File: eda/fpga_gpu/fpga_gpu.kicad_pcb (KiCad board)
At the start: 2 copper layers, 94.5 x 68.3 mm, 57 parts, among them J1 VGA, J2 Bus expansion, U1 ICE40HX4K-TQ144, U2 SST25VF080B-50-4x-S2Ax, U3 74HCT541, U4 74HCT541, U5 74HCT541, U6 TXS0108EPW, U7 TXS0108EPW, U8 AMS1117-3.3, U9 AP2112K-1.2, X1 TXC-7C

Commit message: GPU routing
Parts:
- added U10: IS61C5128AL-10KLI, Package_SO:SOJ-36_10.16x23.49mm_P1.27mm, F.Cu at (43.2, 106.4)
- moved D1 21.8 mm to (60.7, 68.6), turned to 0 degrees
- moved C12 20.8 mm to (43.7, 80.6), turned to 0 degrees
- moved C1 13.5 mm to (56.2, 91.3)
- moved C10 13.5 mm to (65.8, 110.5)
- moved C4 13.5 mm to (63.2, 107.5)
- moved C5 13.5 mm to (74.1, 107.6)
- moved C6 13.5 mm to (83.6, 93.8)
- moved C7 13.5 mm to (56.2, 93.3)
- moved C9 13.5 mm to (83.6, 85.2)
- moved R12 13.5 mm to (90.6, 111.8)
- moved R13 13.5 mm to (90.4, 109.7)
- moved R14 13.5 mm to (90.4, 107.7)
- moved R2 13.5 mm to (92.5, 81.8)
- moved R3 13.5 mm to (94.5, 81.8)
- moved R4 13.5 mm to (90.4, 81.8)
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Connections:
- U1 pad 110: /Interfacing/ADev0 -> /Interfacing/ADev3
- U1 pad 112: /Interfacing/ADev1 -> /Interfacing/ADev2
- U1 pad 113: /Interfacing/ADev2 -> /Interfacing/ADev1
- U1 pad 114: /Interfacing/ADev3 -> /Interfacing/ADev0
- U3 pad 2: /Interfacing/Expansion/A0 -> /Interfacing/Expansion/A3
- U3 pad 3: /Interfacing/Expansion/A1 -> /Interfacing/Expansion/A2
- U3 pad 4: /Interfacing/Expansion/A2 -> /Interfacing/Expansion/A1
- U3 pad 5: /Interfacing/Expansion/A3 -> /Interfacing/Expansion/A0
- U5 pad 11: /Interfacing/Expansion/D7 -> /Interfacing/Expansion/D0
- U5 pad 12: /Interfacing/Expansion/D6 -> /Interfacing/Expansion/D1
- U5 pad 13: /Interfacing/Expansion/D5 -> /Interfacing/Expansion/D2
- U5 pad 14: /Interfacing/Expansion/D4 -> /Interfacing/Expansion/D3
- U5 pad 15: /Interfacing/Expansion/D3 -> /Interfacing/Expansion/D4
- U5 pad 16: /Interfacing/Expansion/D2 -> /Interfacing/Expansion/D5
- U5 pad 17: /Interfacing/Expansion/D1 -> /Interfacing/Expansion/D6
- U5 pad 18: /Interfacing/Expansion/D0 -> /Interfacing/Expansion/D7
- U5 pad 2: /DOut0 -> /DOut7
- U5 pad 3: /DOut1 -> /DOut6
- U5 pad 4: /DOut2 -> /DOut5
- U5 pad 5: /DOut3 -> /DOut4
- U5 pad 6: /DOut4 -> /DOut3
- U5 pad 7: /DOut5 -> /DOut2
- U5 pad 8: /DOut6 -> /DOut1
- U5 pad 9: /DOut7 -> /DOut0
- U7 pad 16: /Interfacing/ADev3 -> /Interfacing/ADev0
- U7 pad 17: /Interfacing/ADev2 -> /Interfacing/ADev1
- U7 pad 18: /Interfacing/ADev1 -> /Interfacing/ADev2
- U7 pad 20: /Interfacing/ADev0 -> /Interfacing/ADev3
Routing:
- net GND: track 5.31 -> 73.2 mm, vias 0 -> 7
- net /DIn0: track 0.00 -> 47.3 mm
- net /DIn1: track 0.00 -> 46.2 mm
- net /DIn2: track 0.00 -> 45.2 mm
- net VCC: track 8.34 -> 52.7 mm
- net /DIn3: track 0.00 -> 44.3 mm
- net +3.3V: track 0.00 -> 43.4 mm
- net /DIn4: track 0.00 -> 43.1 mm
- net /DIn7: track 0.00 -> 42.3 mm
- net /DIn5: track 0.00 -> 41.9 mm
- net /DIn6: track 0.00 -> 40.9 mm
- net /Interfacing/Expansion/A0: track 0.00 -> 40.6 mm
- net /Interfacing/Expansion/A1: track 0.00 -> 33.3 mm
- net /DOut0: track 0.00 -> 33.3 mm
- net /DOut1: track 0.00 -> 32.4 mm
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- added copper zone on B.Cu, net GND

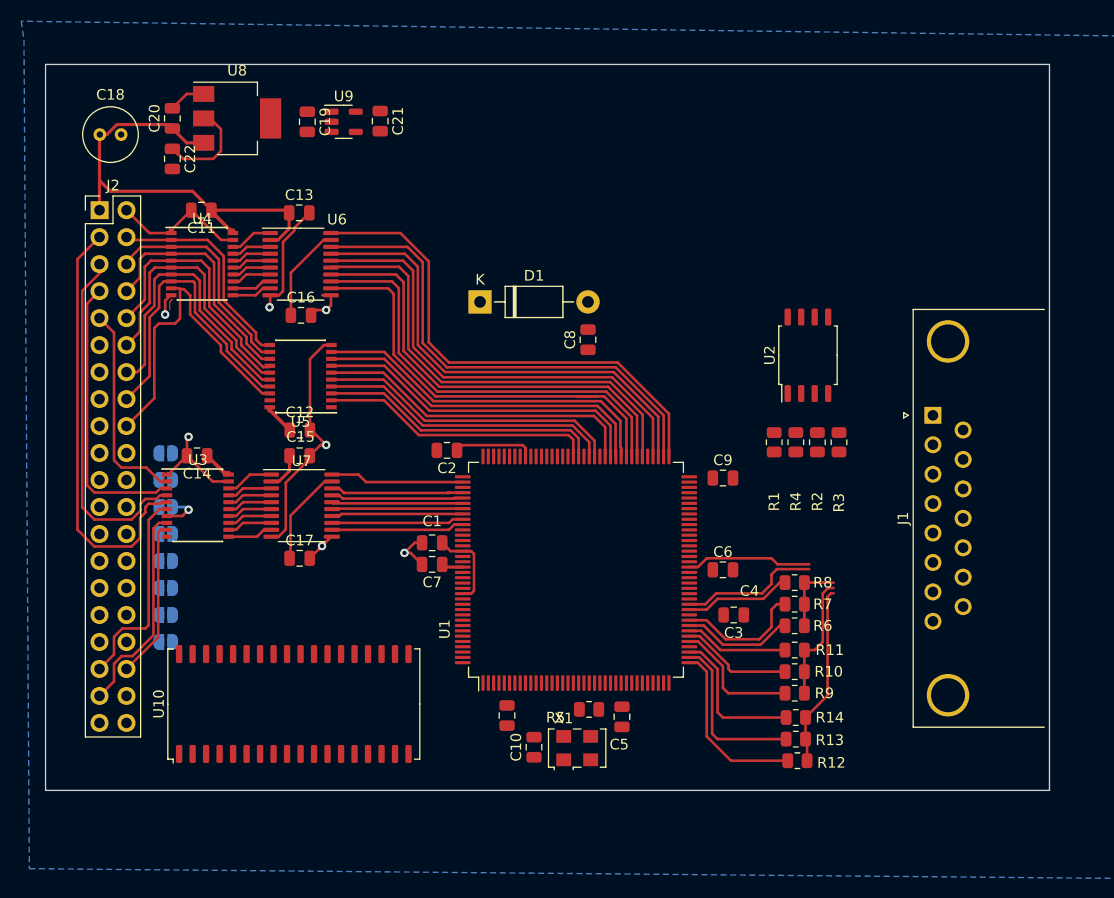
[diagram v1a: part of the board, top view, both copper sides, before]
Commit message: More routing on the GPU board
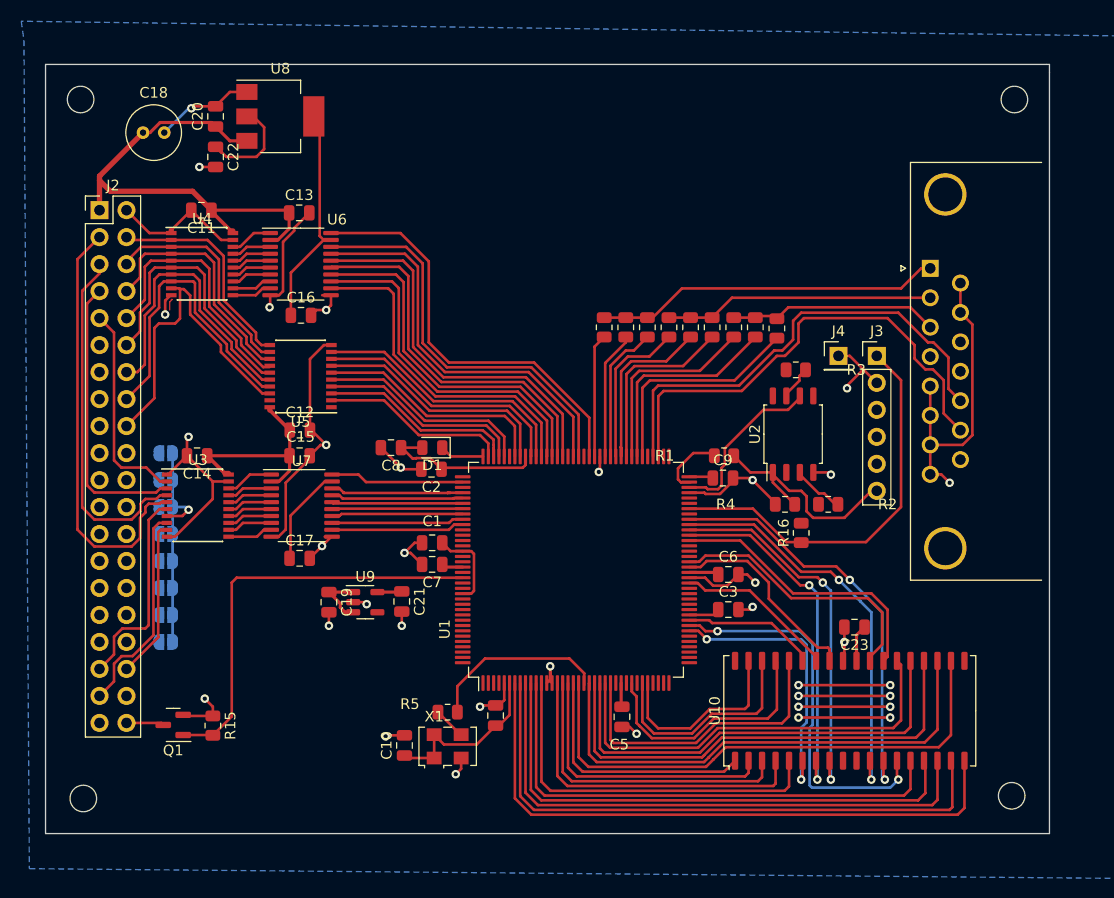
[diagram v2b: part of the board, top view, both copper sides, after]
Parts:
- added C23: 100n, Capacitor_SMD:C_0805_2012Metric, F.Cu at (95.9, 99.2)
- added H1: MountingHole, MountingHole:MountingHole_2.5mm, F.Cu at (111.0, 49.5)
- added H2: MountingHole, MountingHole:MountingHole_2.5mm, F.Cu at (23.1, 49.5)
- added H3: MountingHole, MountingHole:MountingHole_2.5mm, F.Cu at (110.7, 115.1)
- added H4: MountingHole, MountingHole:MountingHole_2.5mm, F.Cu at (23.4, 115.3)
- added J3: programming, Connector_PinHeader_2.54mm:PinHeader_1x06_P2.54mm_Vertical, F.Cu at (98.0, 73.7)
- added J4: reset ground, Connector_PinHeader_2.54mm:PinHeader_1x01_P2.54mm_Vertical, F.Cu at (94.4, 73.7)
- added Q1: 2N7002, Package_TO_SOT_SMD:SOT-23, F.Cu at (31.8, 108.4)
- added R15: 10k, Resistor_SMD:R_0805_2012Metric, F.Cu at (35.6, 108.5)
- added R16: 10k, Resistor_SMD:R_0805_2012Metric, F.Cu at (90.9, 90.3)
- D1: footprint Diode_THT:D_DO-41_SOD81_P10.16mm_Horizontal -> Diode_SMD:D_0805_2012Metric
- moved U10 52.3 mm to (95.5, 107.1)
- moved C19 45.3 mm to (46.5, 96.8)
- moved C21 45.3 mm to (53.3, 96.8)
- moved U9 45.3 mm to (49.9, 96.8)
- moved R12 40.7 mm to (88.6, 71.1), turned to -90 degrees
- moved R13 38.9 mm to (86.6, 71.0), turned to -90 degrees
- moved R14 37.2 mm to (84.6, 71.0), turned to -90 degrees
- moved R9 35.3 mm to (82.5, 71.0), turned to -90 degrees
- moved R10 33.9 mm to (80.5, 71.0), turned to -90 degrees
- moved R11 32.6 mm to (78.5, 71.0), turned to -90 degrees
- moved R6 31.3 mm to (76.5, 71.0), turned to -90 degrees
- moved R7 30.5 mm to (74.4, 71.0), turned to -90 degrees
- moved R8 30.0 mm to (72.4, 71.0), turned to -90 degrees
- moved C8 21.1 mm to (52.3, 82.3), turned to 180 degrees
- moved D1 14.4 mm to (56.2, 82.3), turned to 180 degrees
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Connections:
- J1 pad 13: /HSYNC -> /VSYNC
- J1 pad 14: /VSYNC -> /HSYNC
- J2 pad 40: /Interfacing/Expansion/~{IRQ} -> /Interfacing/~{IRQ}
- U1 pad 10: unconnected-(U1D-IOL_5B-Pad10) -> /RamA6
- U1 pad 101: unconnected-(U1B-IOR_160-Pad101) -> /DOut2
- U1 pad 102: unconnected-(U1B-IOR_161-Pad102) -> /DOut3
- U1 pad 104: unconnected-(U1B-IOR_164-Pad104) -> /DOut4
- U1 pad 105: unconnected-(U1B-IOR_165-Pad105) -> /DOut5
- U1 pad 106: unconnected-(U1B-IOR_166-Pad106) -> /DOut6
- U1 pad 107: unconnected-(U1B-IOR_167-Pad107) -> /DOut7
- U1 pad 11: unconnected-(U1D-IOL_8A-Pad11) -> /RamA5
- U1 pad 12: unconnected-(U1D-IOL_8B-Pad12) -> /RamA4
- U1 pad 128: unconnected-(U1A-IOT_197_GBIN1-Pad128) -> /FpgaIRQ
- U1 pad 15: unconnected-(U1D-IOL_10A-Pad15) -> /RamA3
- U1 pad 16: unconnected-(U1D-IOL_10B-Pad16) -> /RamA2
- U1 pad 17: unconnected-(U1D-IOL_12A-Pad17) -> /RamA1
- U1 pad 18: unconnected-(U1D-IOL_12B-Pad18) -> /RamA0
- U1 pad 19: unconnected-(U1D-IOL_13A-Pad19) -> /RamA10
- U1 pad 21: unconnected-(U1D-IOL_14A_GBIN6-Pad21) -> /RamA11
- U1 pad 22: unconnected-(U1D-IOL_14B-Pad22) -> /RamA12
- U1 pad 23: unconnected-(U1D-IOL_17A-Pad23) -> /RamA13
- U1 pad 24: unconnected-(U1D-IOL_17B-Pad24) -> /RamA14
- U1 pad 25: unconnected-(U1D-IOL_18A-Pad25) -> /RamA15
- U1 pad 29: unconnected-(U1D-IOL_23B-Pad29) -> /RamA16
- U1 pad 31: unconnected-(U1D-IOL_24A-Pad31) -> /RamA17
- U1 pad 32: unconnected-(U1D-IOL_24B-Pad32) -> /RamA18
- U1 pad 37: /VGA Connector/Blue0 -> unconnected-(U1C-IOB_56-Pad37)
- U1 pad 38: /VGA Connector/Blue1 -> unconnected-(U1C-IOB_57-Pad38)
- U1 pad 39: /VGA Connector/Blue2 -> unconnected-(U1C-IOB_61-Pad39)
- U1 pad 41: /VGA Connector/Green0 -> unconnected-(U1C-IOB_63-Pad41)
- U1 pad 42: /VGA Connector/Green1 -> unconnected-(U1C-IOB_64-Pad42)
- U1 pad 43: /VGA Connector/Green2 -> /~{RamCE}
- U1 pad 44: /VGA Connector/Red0 -> /~{RamWE}
- U1 pad 45: /VGA Connector/Red1 -> /~{RamOE}
- U1 pad 47: /VGA Connector/Red2 -> unconnected-(U1C-IOB_79-Pad47)
- U1 pad 48: /VSYNC -> unconnected-(U1C-IOB_80-Pad48)
- U1 pad 52: unconnected-(U1C-IOB_82_GBIN4-Pad52) -> /RamIo7
- U1 pad 55: /HSYNC -> /RamIo6
- U1 pad 56: unconnected-(U1C-IOB_94-Pad56) -> /RamIo5
- U1 pad 60: unconnected-(U1C-IOB_95-Pad60) -> /RamIo4
- U1 pad 61: unconnected-(U1C-IOB_96-Pad61) -> /RamIo0
- U1 pad 62: unconnected-(U1C-IOB_102-Pad62) -> /RamIo1
- U1 pad 63: unconnected-(U1C-IOB_103_CBSEL0-Pad63) -> /RamIo2
- U1 pad 64: unconnected-(U1C-IOB_104_CBSEL1-Pad64) -> /RamIo3
- U1 pad 7: unconnected-(U1D-IOL_4A-Pad7) -> /RamA9
- U1 pad 73: /DIn0 -> unconnected-(U1B-IOR_109-Pad73)
- U1 pad 74: /DIn1 -> unconnected-(U1B-IOR_110-Pad74)
- U1 pad 75: /DIn2 -> /HSYNC
- U1 pad 76: /DIn3 -> /VSYNC
- U1 pad 78: /DIn4 -> /VGA Connector/Blue0
- U1 pad 79: /DIn5 -> /VGA Connector/Blue1
- U1 pad 8: unconnected-(U1D-IOL_4B-Pad8) -> /RamA8
- U1 pad 80: /DIn6 -> /VGA Connector/Blue2
- U1 pad 81: /DIn7 -> /VGA Connector/Green0
- U1 pad 82: /DOut0 -> /VGA Connector/Green1
- U1 pad 83: /DOut1 -> /VGA Connector/Green2
- U1 pad 84: /DOut2 -> /VGA Connector/Red0
- U1 pad 85: /DOut3 -> /VGA Connector/Red1
- U1 pad 87: /DOut4 -> /VGA Connector/Red2
- U1 pad 88: /DOut5 -> /DIn0
- U1 pad 9: unconnected-(U1D-IOL_5A-Pad9) -> /RamA7
- U1 pad 90: /DOut6 -> /DIn1
- U1 pad 91: /DOut7 -> /DIn2
- U1 pad 93: unconnected-(U1B-IOR_140_GBIN3-Pad93) -> /DIn3
- U1 pad 94: unconnected-(U1B-IOR_141_GBIN2-Pad94) -> /DIn4
- U1 pad 95: unconnected-(U1B-IOR_144-Pad95) -> /DIn5
- U1 pad 96: unconnected-(U1B-IOR_146-Pad96) -> /DIn6
- U1 pad 97: unconnected-(U1B-IOR_147-Pad97) -> /DIn7
- U1 pad 98: unconnected-(U1B-IOR_148-Pad98) -> /DOut0
- U1 pad 99: unconnected-(U1B-IOR_152-Pad99) -> /DOut1
- U10 pad 1: unconnected-(U10-A0-Pad1) -> /RamA0
- U10 pad 11: unconnected-(U10-I/O2-Pad11) -> /RamIo2
- U10 pad 12: unconnected-(U10-I/O3-Pad12) -> /RamIo3
- U10 pad 13: unconnected-(U10-~{WE}-Pad13) -> /~{RamWE}
- U10 pad 14: unconnected-(U10-A5-Pad14) -> /RamA5
- U10 pad 15: unconnected-(U10-A6-Pad15) -> /RamA6
- U10 pad 16: unconnected-(U10-A7-Pad16) -> /RamA7
- U10 pad 17: unconnected-(U10-A8-Pad17) -> /RamA8
- U10 pad 18: unconnected-(U10-A9-Pad18) -> /RamA9
- U10 pad 2: unconnected-(U10-A1-Pad2) -> /RamA1
- U10 pad 20: unconnected-(U10-A10-Pad20) -> /RamA10
- U10 pad 21: unconnected-(U10-A11-Pad21) -> /RamA11
- U10 pad 22: unconnected-(U10-A12-Pad22) -> /RamA12
- U10 pad 23: unconnected-(U10-A13-Pad23) -> /RamA13
- U10 pad 24: unconnected-(U10-A14-Pad24) -> /RamA14
- U10 pad 25: unconnected-(U10-I/O4-Pad25) -> /RamIo4
- U10 pad 26: unconnected-(U10-I/O5-Pad26) -> /RamIo5
- U10 pad 27: Net-(U10-VDD-Pad27) -> VCC
- U10 pad 29: unconnected-(U10-I/O6-Pad29) -> /RamIo6
- U10 pad 3: unconnected-(U10-A2-Pad3) -> /RamA2
- U10 pad 30: unconnected-(U10-I/O7-Pad30) -> /RamIo7
- U10 pad 31: unconnected-(U10-~{OE}-Pad31) -> /~{RamOE}
- U10 pad 32: unconnected-(U10-A15-Pad32) -> /RamA15
- U10 pad 33: unconnected-(U10-A16-Pad33) -> /RamA16
- U10 pad 34: unconnected-(U10-A17-Pad34) -> /RamA17
- U10 pad 35: unconnected-(U10-A18-Pad35) -> /RamA18
- U10 pad 4: unconnected-(U10-A3-Pad4) -> /RamA3
- U10 pad 5: unconnected-(U10-A4-Pad5) -> /RamA4
- U10 pad 6: unconnected-(U10-~{CE}-Pad6) -> /~{RamCE}
- U10 pad 7: unconnected-(U10-I/O0-Pad7) -> /RamIo0
- U10 pad 8: unconnected-(U10-I/O1-Pad8) -> /RamIo1
- U10 pad 9: Net-(U10-VDD-Pad27) -> VCC
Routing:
- net GND: track 73.2 -> 210.3 mm, vias 7 -> 35
- net /RamA9: track 0.00 -> 58.5 mm
- net /RamA8: track 0.00 -> 56.4 mm
- net /RamA7: track 0.00 -> 53.5 mm
- net /RamA6: track 0.00 -> 51.0 mm
- net /RamA10: track 0.00 -> 50.6 mm
- net /RamA5: track 0.00 -> 48.3 mm
- net /RamA11: track 0.00 -> 47.6 mm
- net /RamA12: track 0.00 -> 45.2 mm
- net /RamA13: track 0.00 -> 42.8 mm
- net +3.3V: track 43.4 -> 84.9 mm
- net /RamA14: track 0.00 -> 40.5 mm
- net /FpgaIRQ: track 0.00 -> 39.8 mm
- net /RamIo3: track 0.00 -> 39.5 mm, vias 0 -> 2
- net /RamIo2: track 0.00 -> 38.1 mm, vias 0 -> 2
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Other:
- board size 94.5 x 68.3 mm -> 94.5 x 72.4 mm

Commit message: Update eda
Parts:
- added SW1: SW_Reset, Button_Switch_SMD:SW_SPST_TL3305A, F.Cu at (91.9, 52.3)
- added SW2: SW_FlashPwrCycle, Button_Switch_SMD:SW_SPST_TL3305A, F.Cu at (82.0, 52.3)
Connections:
- R2 pad 2: +3.3V -> Net-(SW2-A)
- R3 pad 2: +3.3V -> Net-(SW2-A)
- U2 pad 8: +3.3V -> Net-(SW2-A)
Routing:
- net VCC: track 73.8 -> 278.1 mm, vias 0 -> 10
- net +3.3V: track 84.9 -> 252.4 mm, vias 0 -> 9
- net +1V2: track 9.42 -> 77.1 mm, vias 0 -> 8
- net Net-(SW2-A): track 0.00 -> 51.6 mm, vias 0 -> 2
- net unconnected-(J1-Pad0): track 0.00 -> 37.2 mm
- net ice40-SDO: track 0.00 -> 28.5 mm, vias 0 -> 1
- net ice40-CRESET: track 37.8 -> 65.3 mm, vias 0 -> 1
- net GND: track 210.3 -> 235.2 mm, vias 35 -> 47
- net ice40-SDI: track 0.00 -> 24.7 mm, vias 0 -> 3
- net ice40-SCK: track 16.1 -> 26.5 mm, vias 0 -> 2
- net /Interfacing/Expansion/D7: track 30.7 -> 29.8 mm
- net /Interfacing/~{RST}: track 12.5 -> 13.2 mm
- net /Interfacing/R~{W}: track 12.4 -> 13.1 mm
- net /Interfacing/~{CS}: track 12.4 -> 13.0 mm
- net /Interfacing/Clock: track 12.3 -> 12.9 mm
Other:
- board text added: "A0"
- board text added: "A1"
- board text added: "A10"
- board text added: "A11"
- board text added: "A12"
- board text added: "A13"
- board text added: "A14"
- board text added: "A15"
- board text added: "A2"
- board text added: "A3"
- board text added: "A4"
- board text added: "A5"
- board text added: "A6"
- board text added: "A7"
- board text added: "A8"
- board text added: "A9"
- board text added: "CLK"
- board text added: "D0"
- board text added: "D1"
- board text added: "D2"
- board text added: "D3"
- board text added: "D4"
- board text added: "D5"
- board text added: "D6"
- board text added: "D7"
- board text added: "FPGA Reset"
- board text added: "Flash Pwr Cycle"
- board text added: "GND"
- board text added: "Niklas Hedlund - 2023"
- board text added: "Project WRASS, GPU - v1.0"
- board text added: "Reset"
- board text added: "R~{W}"
- board text added: "SCK"
- board text added: "SDI"
- board text added: "SDO"
- board text added: "To program, bridge the reset line with the gnd pin. Then pwr cycle the flash"
- board text added: "VCC"
- board text added: "~{CS}"
- board text added: "~{DMA}"
- board text added: "~{IRQ}"
- board text added: "~{NMI}"
- board text added: "~{RST}"
